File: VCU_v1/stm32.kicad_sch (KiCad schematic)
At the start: 0 parts

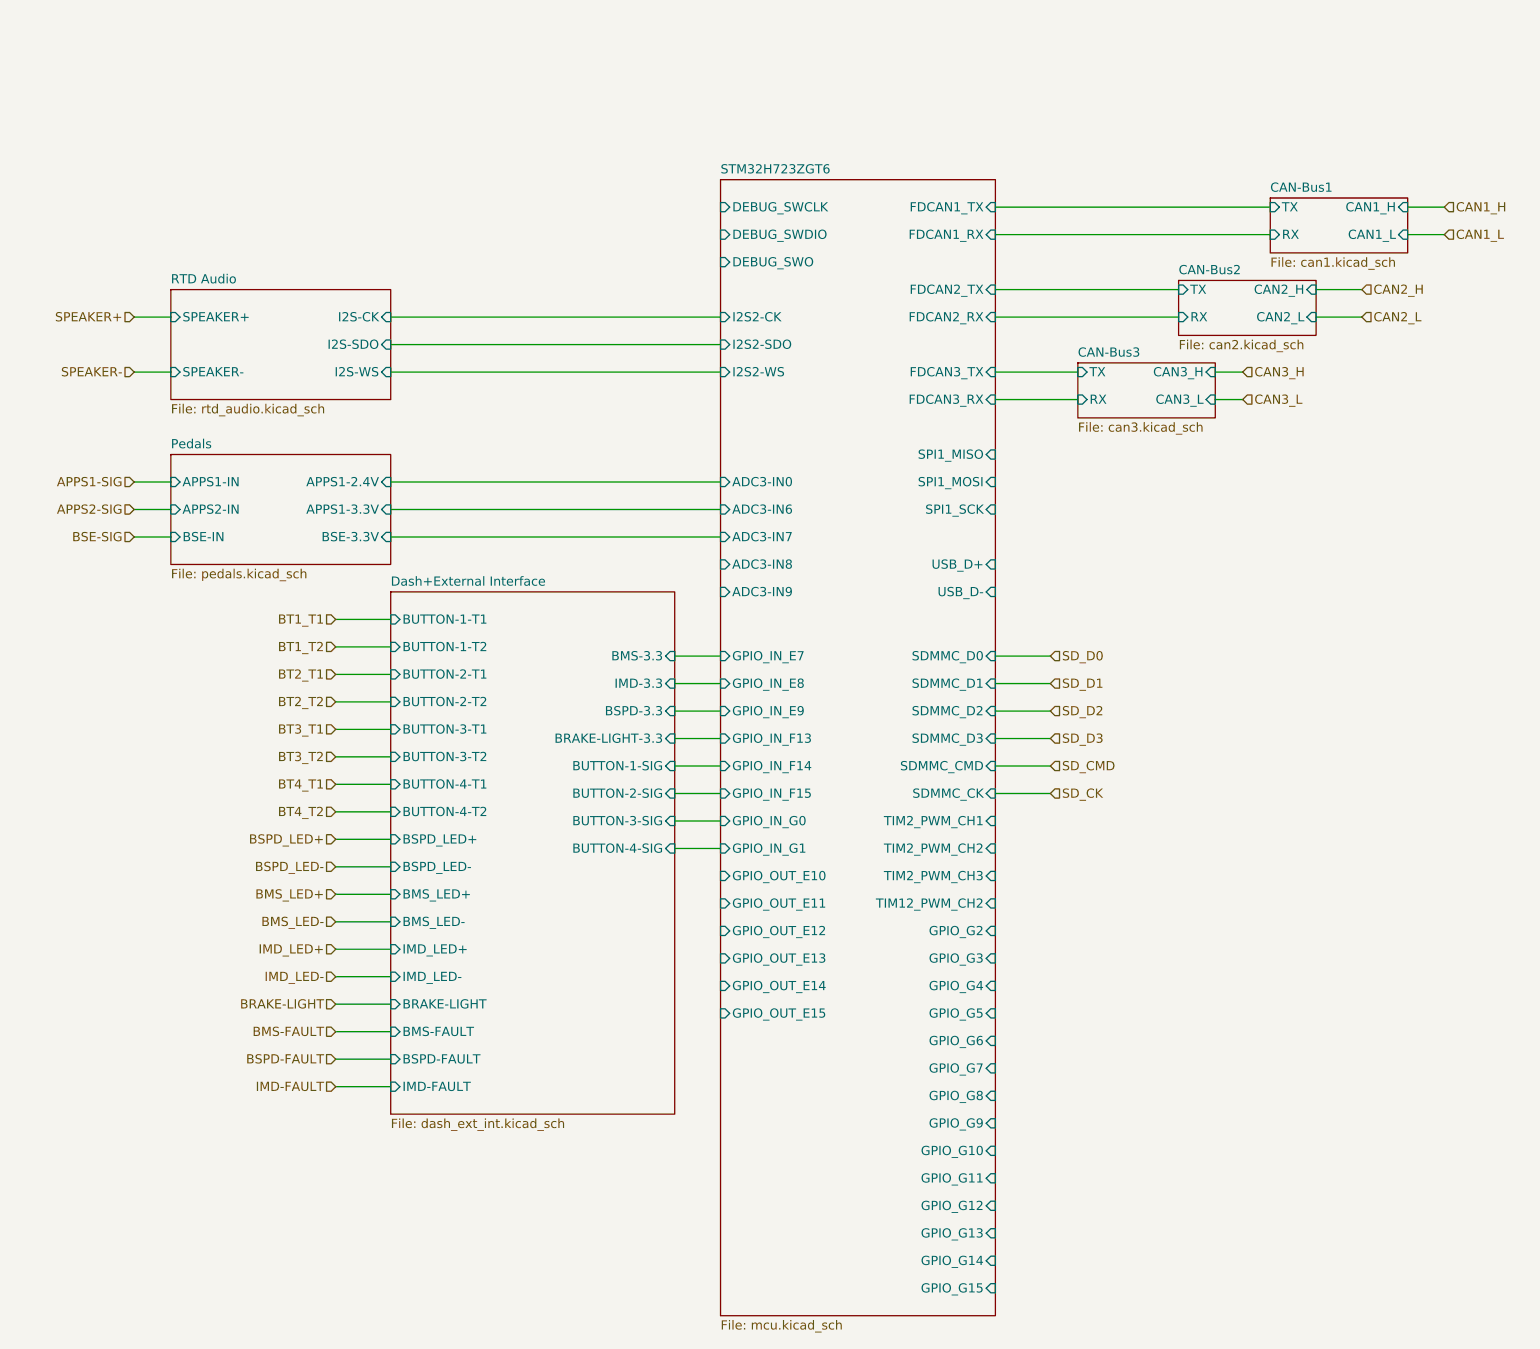
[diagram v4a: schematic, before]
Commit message: v1 schematic (actually) complete, let the layout commence
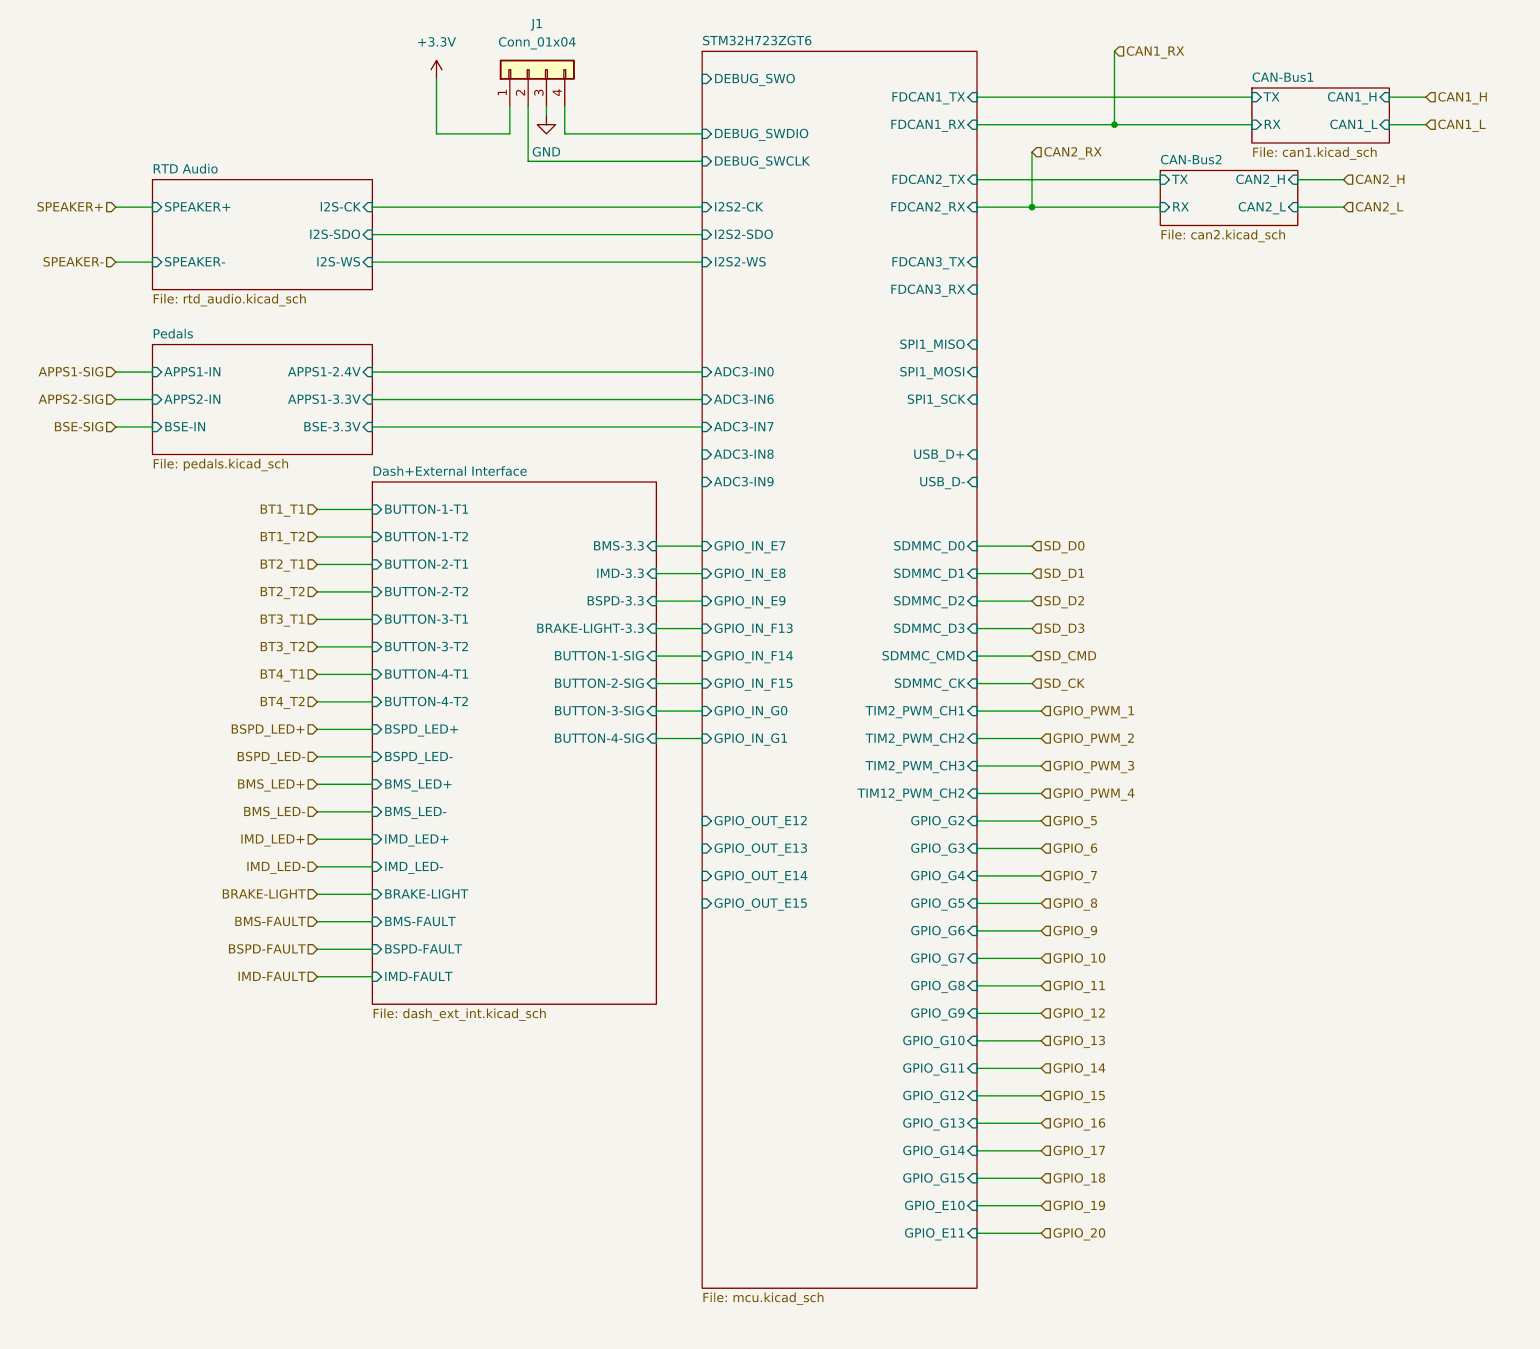
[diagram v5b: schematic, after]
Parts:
- added J1: Conn_01x04, Connector_PinHeader_2.54mm:PinHeader_1x04_P2.54mm_Vertical, symbol Connector_Generic:Conn_01x04
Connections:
- net STM32H723ZGT6/DEBUG_SWCLK: now also J1.2 (Pin_2)
- net STM32H723ZGT6/DEBUG_SWDIO: now also J1.4 (Pin_4)
- new net +3.3V: J1.1 (Pin_1)
- new net GND: J1.3 (Pin_3)
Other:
- removed sheet CAN-Bus3
- sheet STM32H723ZGT6 ports: added GPIO_E10, GPIO_E11; removed GPIO_OUT_E10, GPIO_OUT_E11

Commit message: begin pcb design
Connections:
- no-connect marks 0 -> 14
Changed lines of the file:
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@@
 		(color 0 0 0 0)
+	)
+	(no_connect
+		(at 110.49 140.97)
+	)
+	(no_connect
+		(at 148.59 67.31)
+	)
+	(no_connect
+		(at 110.49 26.67)
+	)
+	(no_connect
+		(at 110.49 78.74)
+	)
+	(no_connect
+		(at 148.59 63.5)
+	)
+	(no_connect
+		(at 148.59 52.07)
+	)
+	(no_connect
+		(at 110.49 82.55)
+	)
+	(no_connect
+		(at 110.49 129.54)
+	)
+	(no_connect
+		(at 148.59 78.74)
+	)
+	(no_connect
+		(at 148.59 55.88)
+	)
+	(no_connect
+		(at 148.59 82.55)
+	)
+	(no_connect
+		(at 148.59 71.12)
+	)
+	(no_connect
+		(at 110.49 133.35)
+	)
+	(no_connect
+		(at 110.49 137.16)
 	)
 	(wire
